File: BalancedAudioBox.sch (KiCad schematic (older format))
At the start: 5 parts, among them J1 Conn_02x10_Odd_Even, J2 Conn_01x02, J5 Conn_01x03, J7 Conn_01x05

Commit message: larger conn
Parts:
- J7: value Conn_01x05 -> Conn_01x06; footprint Connector_PinHeader_2.54mm:PinHeader_1x05_P2.54mm_Vertical -> Connector_PinHeader_2.54mm:PinHeader_1x06_P2.54mm_Vertical; symbol Connector_Generic:Conn_01x05 -> Connector_Generic:Conn_01x06
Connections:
- net +3V3: now also J7.5 (Pin_5)
- net GND: now also J7.6 (Pin_6); no longer J7.5 (Pin_5)
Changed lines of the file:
@@
 MCLK
 $Comp
-L Connector_Generic:Conn_01x05 J7
+L Connector_Generic:Conn_01x06 J7
 U 1 1 5D4691F7
 P 3000 4300
 F 0 "J7" H 2918 4717 50  0000 C CNN
-F 1 "Conn_01x05" H 2918 4626 50  0000 C CNN
-F 2 "Connector_PinHeader_2.54mm:PinHeader_1x05_P2.54mm_Vertical" H 3000 4300 50  0001 C CNN
+F 1 "Conn_01x06" H 2918 4626 50  0000 C CNN
+F 2 "Connector_PinHeader_2.54mm:PinHeader_1x06_P2.54mm_Vertical" H 3000 4300 50  0001 C CNN
 F 3 "~" H 3000 4300 50  0001 C CNN
 	1    3000 4300
@@
 	1    0    0    -1
 $EndComp
-Wire Wire Line
-	3200 4500 3300 4500
-Wire Wire Line
-	3300 4500 3300 4650
 Text GLabel 3950 5950 1    50   Input ~ 0
 VIN
@@
 	-1   0    0    1
 $EndComp
+Wire Wire Line
+	3200 4600 3300 4600
+Wire Wire Line
+	3300 4600 3300 4650
+$Comp
+L power:+3.3V #PWR0101
+U 1 1 5DDD4DCB
+P 3550 4450
+F 0 "#PWR0101" H 3550 4300 50  0001 C CNN
+F 1 "+3.3V" H 3565 4623 50  0000 C CNN
+F 2 "" H 3550 4450 50  0001 C CNN
+F 3 "" H 3550 4450 50  0001 C CNN
+	1    3550 4450
+	1    0    0    -1
+$EndComp
+Wire Wire Line
+	3200 4500 3550 4500
+Wire Wire Line
+	3550 4500 3550 4450
 $EndSCHEMATC

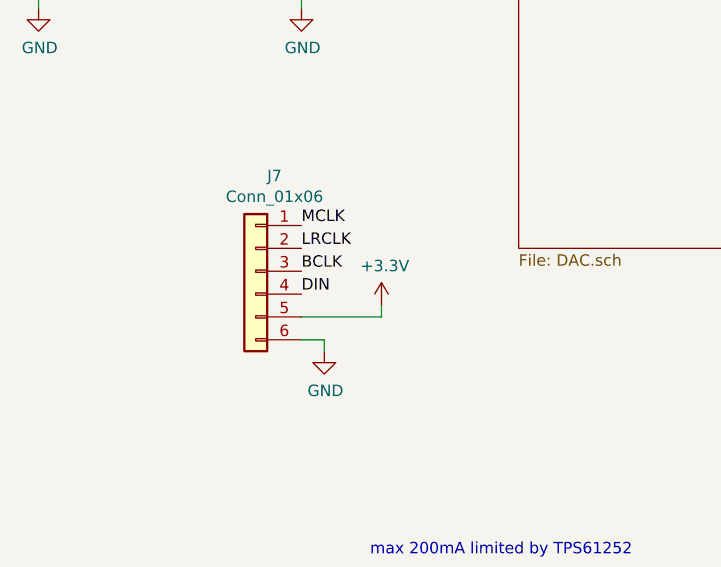
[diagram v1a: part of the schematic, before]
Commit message: smaller package, drc
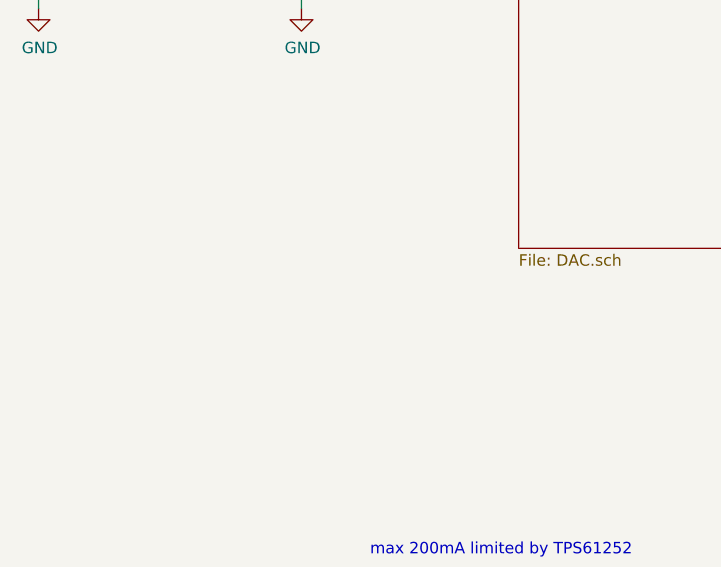
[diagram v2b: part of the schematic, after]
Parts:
- removed J7: Conn_01x06, Connector_PinHeader_2.54mm:PinHeader_1x06_P2.54mm_Vertical, symbol Connector_Generic:Conn_01x06
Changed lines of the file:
@@
 Text Label 3400 2400 0    50   ~ 0
 MCLK
-$Comp
-L Connector_Generic:Conn_01x06 J7
-U 1 1 5D4691F7
-P 3000 4300
-F 0 "J7" H 2918 4717 50  0000 C CNN
-F 1 "Conn_01x06" H 2918 4626 50  0000 C CNN
-F 2 "Connector_PinHeader_2.54mm:PinHeader_1x06_P2.54mm_Vertical" H 3000 4300 50  0001 C CNN
-F 3 "~" H 3000 4300 50  0001 C CNN
-	1    3000 4300
-	-1   0    0    -1
-$EndComp
-Text Label 3200 4100 0    50   ~ 0
-MCLK
-Text Label 3200 4200 0    50   ~ 0
-LRCLK
-Text Label 3200 4300 0    50   ~ 0
-BCLK
-Text Label 3200 4400 0    50   ~ 0
-DIN
-$Comp
-L power:GND #PWR0102
-U 1 1 5D46AD06
-P 3300 4650
-F 0 "#PWR0102" H 3300 4400 50  0001 C CNN
-F 1 "GND" H 3305 4477 50  0000 C CNN
-F 2 "" H 3300 4650 50  0001 C CNN
-F 3 "" H 3300 4650 50  0001 C CNN
-	1    3300 4650
-	1    0    0    -1
-$EndComp
 Text GLabel 3950 5950 1    50   Input ~ 0
 VIN
@@
 	-1   0    0    1
 $EndComp
-Wire Wire Line
-	3200 4600 3300 4600
-Wire Wire Line
-	3300 4600 3300 4650
-$Comp
-L power:+3.3V #PWR0101
-U 1 1 5DDD4DCB
-P 3550 4450
-F 0 "#PWR0101" H 3550 4300 50  0001 C CNN
-F 1 "+3.3V" H 3565 4623 50  0000 C CNN
-F 2 "" H 3550 4450 50  0001 C CNN
-F 3 "" H 3550 4450 50  0001 C CNN
-	1    3550 4450
-	1    0    0    -1
-$EndComp
-Wire Wire Line
-	3200 4500 3550 4500
-Wire Wire Line
-	3550 4500 3550 4450
 $EndSCHEMATC
